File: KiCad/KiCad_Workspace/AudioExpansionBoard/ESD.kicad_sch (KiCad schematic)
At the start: 8 parts, among them J1 AudioJack2

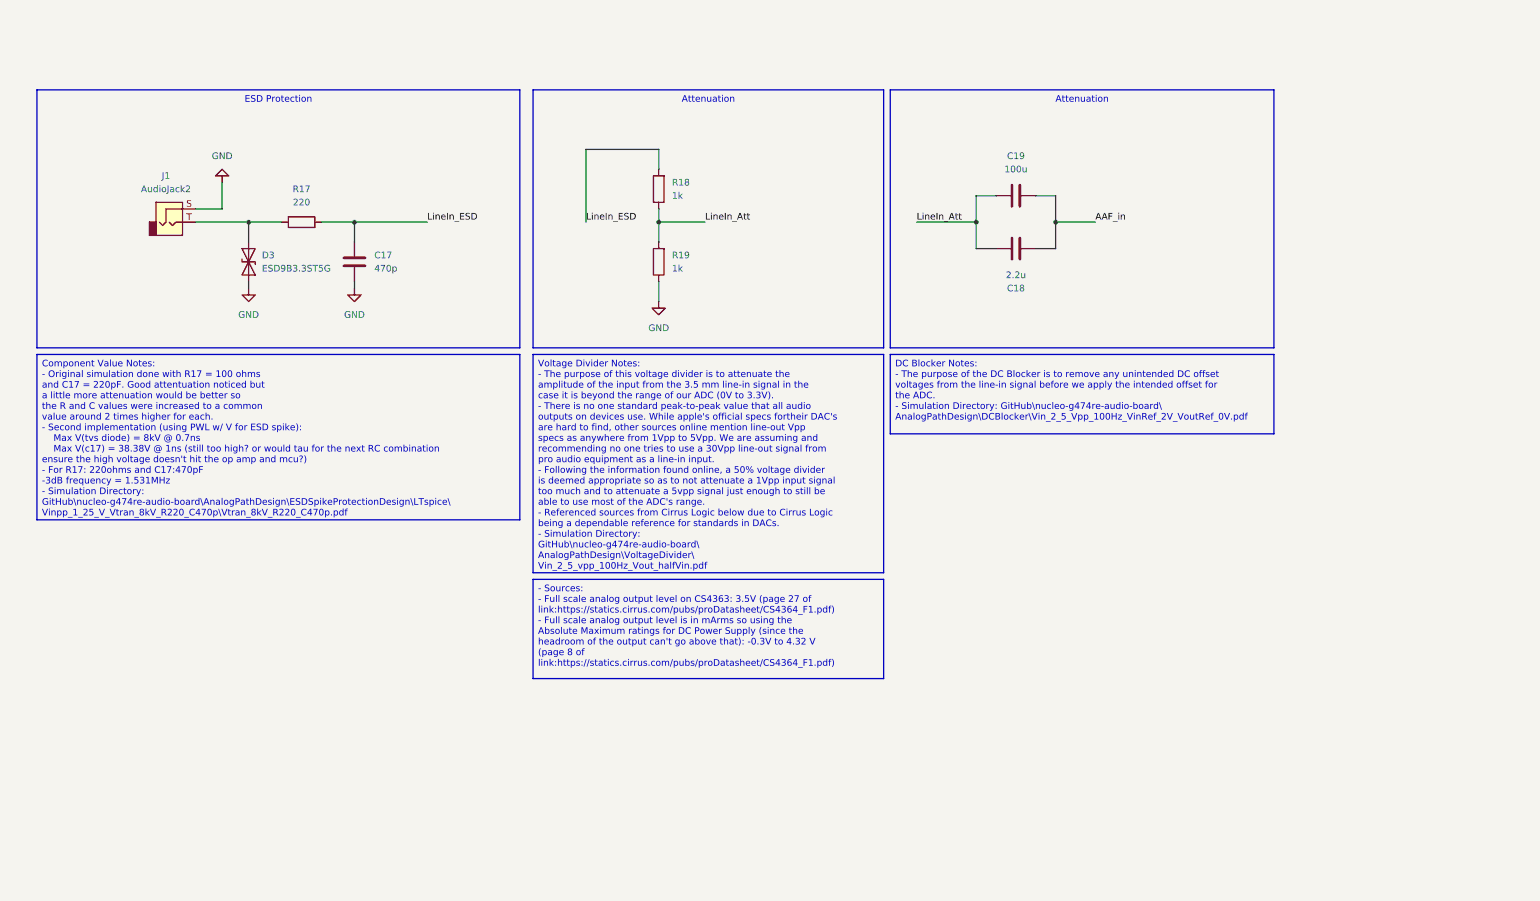
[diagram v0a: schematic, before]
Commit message: Added to designs to schematic and simulations
Added sections to analog line-in path (Offset and Voltage Divider). Moved the Sallen-Key Anti-Aliasing Filter to the line-in path schematic and added simulations (in LTspice) for each section of the analog line-in path.
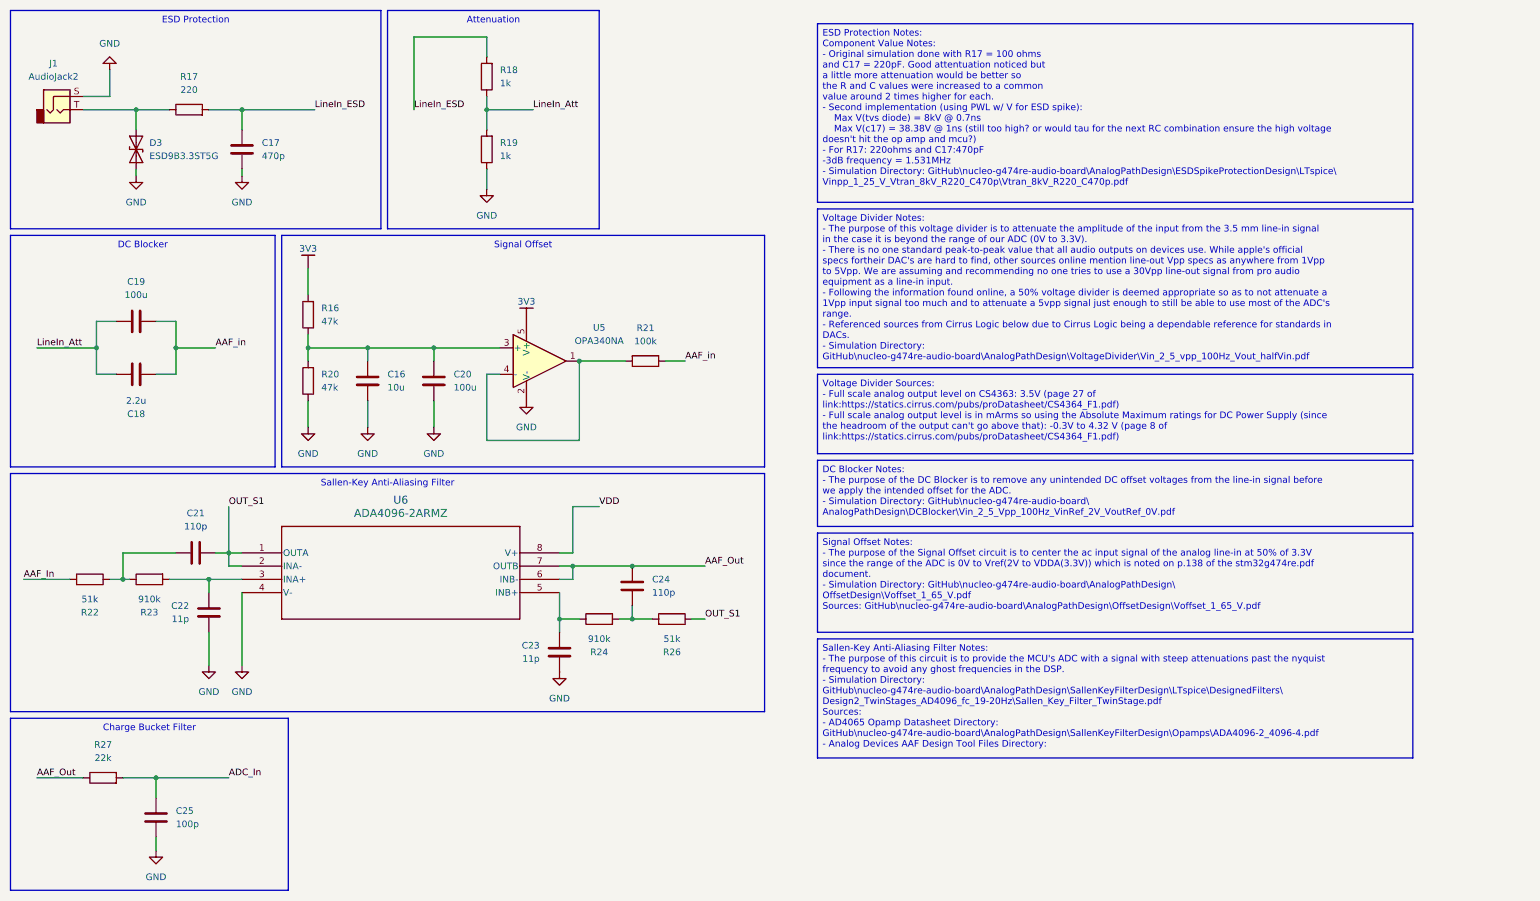
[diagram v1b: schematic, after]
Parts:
- added C16: 10u, symbol Device:C
- added C20: 100u, symbol Device:C
- added C21, C24: 110p, symbol Device:C
- added C22, C23: 11p, symbol Device:C
- added C25: 100p, symbol Device:C
- added R16, R20: 47k, symbol Device:R
- added R21: 100k, symbol Device:R
- added R22, R26: 51k, symbol Device:R
- added R23, R24: 910k, symbol Device:R
- added R27: 22k, symbol Device:R
- added U5: OPA340NA, Package_TO_SOT_SMD:SOT-23-5, symbol Amplifier_Operational:OPA340NA
- added U6: ADA4096-2ARMZ, RM_8_ADI, symbol ADA4096-2ARMZ:ADA4096-2ARMZ
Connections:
- net AAF_in: now also R21.1
- net GND: now also C16.2, C20.2, C22.2, C23.2, C25.1, R20.1, U5.2 (V-), U6.4 (V-)
- new net: C22.1, R23.2, U6.3 (INA+)
- new net: R21.2, U5.1, U5.4 (-)
- new net: C16.1, C20.1, R16.1, R20.2, U5.3 (+)
- new net: C21.1, R22.1, R23.1
- new net: C23.1, R24.1, U6.5 (INB+)
- new net: C24.1, R24.2, R26.2
- new net 3V3: R16.2, U5.5 (V+)
- new net AAF_In: R22.2
- new net AAF_Out: C24.2, R27.1, U6.6 (INB-), U6.7 (OUTB)
- new net ADC_In: C25.2, R27.2
- new net OUT_S1: C21.2, R26.1, U6.1 (OUTA), U6.2 (INA-)
- new net VDD: U6.8 (V+)
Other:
- moved on the sheet: C17, C18, C19, D3, J1, R17, R18, R19
